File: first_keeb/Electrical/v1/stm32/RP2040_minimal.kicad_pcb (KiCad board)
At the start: 4 copper layers, 67.1 x 66.8 mm, 71 parts, among them J1 Conn_01x04_Socket, P1 USB-TYPE-C-016, Q1 BSS138, SW1 TS-1187A-B-A-B, SW2 TS-1187A-B-A-B, SW3 BUTT1, SW4 BUTT3, SW5 BUTT2, U1 ME6208A44M3G, U2 ME6212C25M5G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

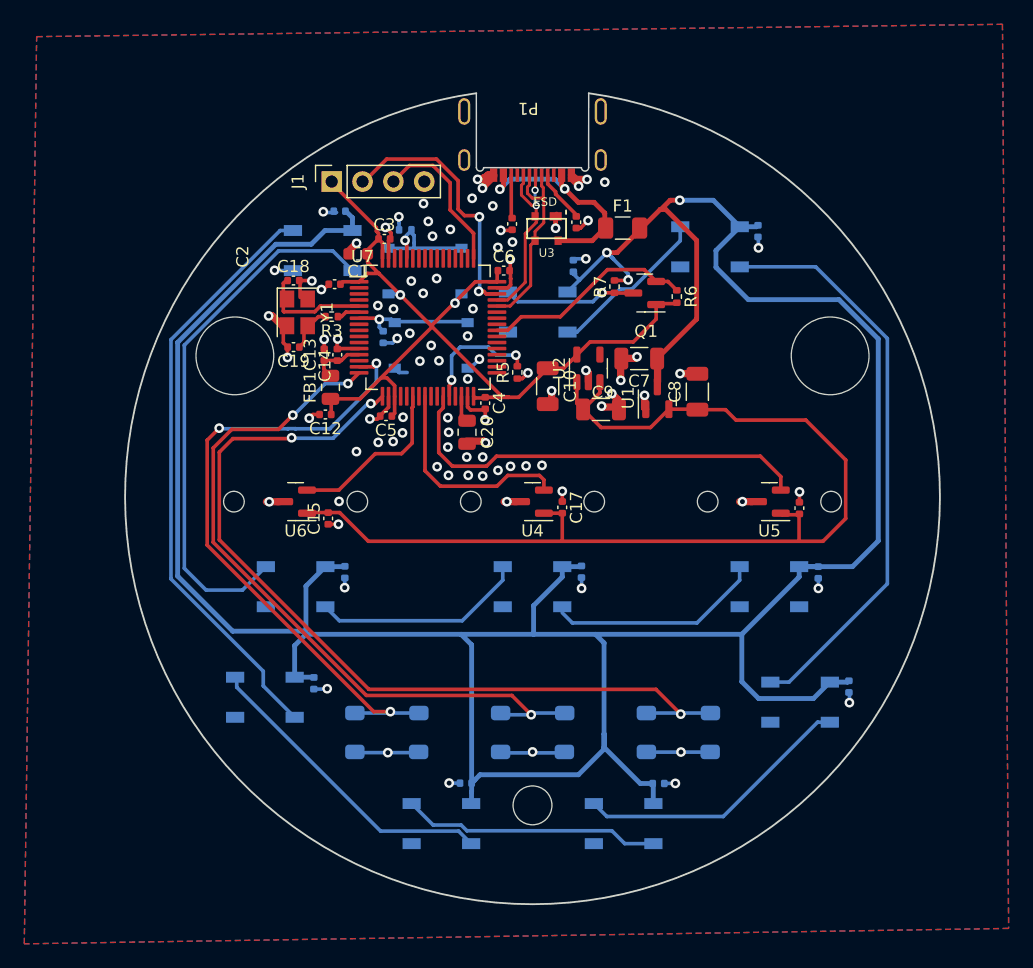
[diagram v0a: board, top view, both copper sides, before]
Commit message: switches swdio and swclk on stm to match rp2040
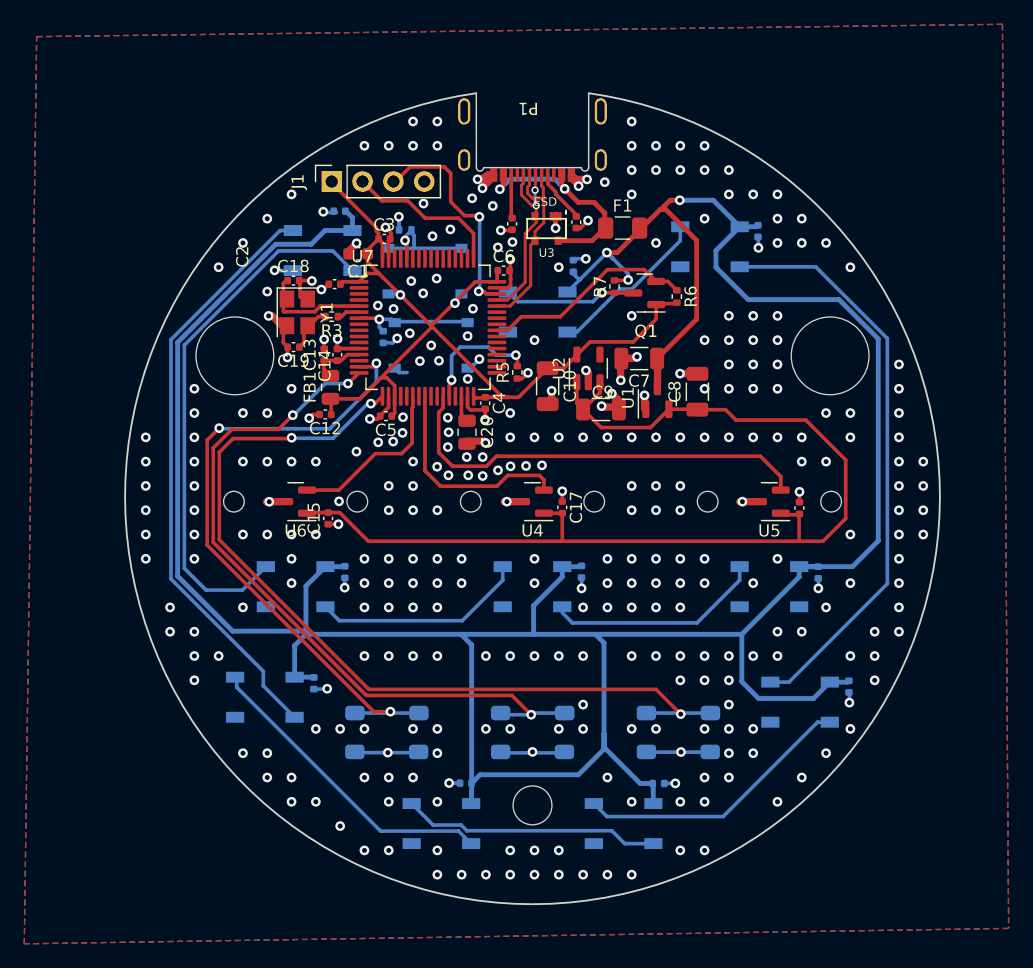
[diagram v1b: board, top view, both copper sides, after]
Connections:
- J1 pad 2: SWDIO -> SWCLK
- J1 pad 3: SWCLK -> SWDIO
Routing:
- net SWDIO: track 21.5 -> 18.4 mm
- net GND: vias 92 -> 341

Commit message: generates assembly files
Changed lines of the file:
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@@
     (fp_line (start 1.6 0.8) (end -1.6 0.8)
       (stroke (width 0.1) (type solid)) (layer "F.Fab"))
-    (pad "1" smd roundrect (at -1.475 0 90) (size 1.15 1.8) (layers "F.Cu" "F.Paste" "F.Mask") (roundrect_rratio 0.217391)
+    (pad "1" smd roundrect (at -1.475 0 90) (size 1.15 1.8) (layers "F.Cu" "F.Paste" "F.Mask") (roundrect_rratio 0.2173913043)
       (net 70 "+4V4") (pintype "passive"))
-    (pad "2" smd roundrect (at 1.475 0 90) (size 1.15 1.8) (layers "F.Cu" "F.Paste" "F.Mask") (roundrect_rratio 0.217391)
+    (pad "2" smd roundrect (at 1.475 0 90) (size 1.15 1.8) (layers "F.Cu" "F.Paste" "F.Mask") (roundrect_rratio 0.2173913043)
       (net 1 "GND") (pintype "passive"))
     (model "${KICAD6_3DMODEL_DIR}/Capacitor_SMD.3dshapes/C_1206_3216Metric.wrl"

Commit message: make bottom hole
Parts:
- H3: value MountingHole_3.2mm_M3_DIN965 -> MountingHole_4.3mm_M4_DIN965; footprint MountingHole:MountingHole_3.2mm_M3_DIN965 -> MountingHole:MountingHole_4.3mm_M4_DIN965
- moved H1 1.00 mm to (123.5, 88.0)
- moved H2 1.00 mm to (76.5, 88.0)
- moved R3 0.41 mm to (83.7, 85.1)
- moved C18 0.40 mm to (80.7, 81.7)
- moved C19 0.40 mm to (80.7, 87.2)
- moved Y1 0.40 mm to (81.0, 84.4)
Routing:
- net OSC_IN: track 9.25 -> 8.01 mm
- net GND: track 88.0 -> 88.6 mm, vias 341 -> 340
